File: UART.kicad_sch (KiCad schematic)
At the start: 28 parts, among them J22 430450212, J23 430450612, J24 430450212, J9 Conn_01x03_Pin, U5 MAX485, U7 ISOW1432BDFMR

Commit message: Pre Design Review - Reviewed DRC Errors
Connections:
- net +3V3_TB: now also R20.2
- net +5V_TB: no longer R20.2
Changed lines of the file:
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@@
 			)
 		)
-		(property "Value" "+5V_TB"
+		(property "Value" "+3V3_TB"
 			(at 138.43 81.534 0)
 			(effects

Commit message: Hello Bruh
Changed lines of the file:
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@@
-	)
-	(junction
-		(at 254 107.95)
-		(diameter 0)
-		(color 0 0 0 0)
 	)
 	(junction
@@
 	(junction
 		(at 69.85 77.47)
-		(diameter 0)
-		(color 0 0 0 0)
-	)
-	(junction
-		(at 254 110.49)
 		(diameter 0)
 		(color 0 0 0 0)
@@
 	(wire
 		(pts
-			(xy 254 110.49) (xy 254 114.3)
-		)
-		(stroke
-			(width 0)
-			(type default)
-		)
-	)
-	(wire
-		(pts
 			(xy 123.19 66.04) (xy 129.54 66.04)
 		)
@@
 	(wire
 		(pts
+			(xy 251.46 107.95) (xy 256.54 107.95)
+		)
+		(stroke
+			(width 0)
+			(type default)
+		)
+	)
+	(wire
+		(pts
 			(xy 71.12 116.84) (xy 77.47 116.84)
 		)
@@
 	(wire
 		(pts
-			(xy 251.46 107.95) (xy 254 107.95)
-		)
-		(stroke
-			(width 0)
-			(type default)
-		)
-	)
-	(wire
-		(pts
 			(xy 133.35 113.03) (xy 139.7 113.03)
 		)
@@
 	(wire
 		(pts
-			(xy 254 107.95) (xy 256.54 107.95)
-		)
-		(stroke
-			(width 0)
-			(type default)
-		)
-	)
-	(wire
-		(pts
 			(xy 116.84 91.44) (xy 119.38 91.44)
 		)
@@
 	(wire
 		(pts
-			(xy 254 105.41) (xy 254 107.95)
-		)
-		(stroke
-			(width 0)
-			(type default)
-		)
-	)
-	(wire
-		(pts
 			(xy 173.99 134.62) (xy 175.26 134.62)
 		)
@@
 	(wire
 		(pts
-			(xy 245.11 110.49) (xy 254 110.49)
+			(xy 245.11 110.49) (xy 256.54 110.49)
 		)
 		(stroke
@@
 		(pts
 			(xy 71.12 125.73) (xy 71.12 127)
-		)
-		(stroke
-			(width 0)
-			(type default)
-		)
-	)
-	(wire
-		(pts
-			(xy 254 110.49) (xy 256.54 110.49)
 		)
 		(stroke
@@
 	)
 	(label "A"
-		(at 254 114.3 0)
+		(at 241.3 110.49 0)
 		(fields_autoplaced yes)
 		(effects
@@
 	)
 	(label "B"
-		(at 254 105.41 0)
+		(at 241.3 107.95 0)
 		(fields_autoplaced yes)
 		(effects

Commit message: Fixed MAX485 Schematic
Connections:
- net +5V: now also C14.2, U5.8 (VCC)
- net A: no longer C14.2, U5.8 (VCC)
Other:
- moved on the sheet: R10
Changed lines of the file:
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@@
 	)
 	(junction
+		(at 251.46 87.63)
+		(diameter 0)
+		(color 0 0 0 0)
+	)
+	(junction
 		(at 129.54 73.66)
 		(diameter 0)
@@
 	)
 	(junction
-		(at 245.11 105.41)
-		(diameter 0)
-		(color 0 0 0 0)
-	)
-	(junction
 		(at 119.38 91.44)
 		(diameter 0)
@@
 	(wire
 		(pts
+			(xy 245.11 87.63) (xy 251.46 87.63)
+		)
+		(stroke
+			(width 0)
+			(type default)
+		)
+	)
+	(wire
+		(pts
 			(xy 116.84 71.12) (xy 116.84 73.66)
 		)
@@
 	(wire
 		(pts
-			(xy 238.76 105.41) (xy 245.11 105.41)
+			(xy 238.76 105.41) (xy 251.46 105.41)
 		)
 		(stroke
@@
 	(wire
 		(pts
+			(xy 251.46 83.82) (xy 251.46 87.63)
+		)
+		(stroke
+			(width 0)
+			(type default)
+		)
+	)
+	(wire
+		(pts
 			(xy 77.47 99.06) (xy 77.47 100.33)
 		)
@@
 	(wire
 		(pts
+			(xy 245.11 87.63) (xy 245.11 90.17)
+		)
+		(stroke
+			(width 0)
+			(type default)
+		)
+	)
+	(wire
+		(pts
 			(xy 139.7 114.3) (xy 139.7 113.03)
 		)
@@
 	(wire
 		(pts
-			(xy 116.84 93.98) (xy 116.84 91.44)
+			(xy 251.46 87.63) (xy 251.46 105.41)
 		)
 		(stroke
@@
 	(wire
 		(pts
-			(xy 245.11 110.49) (xy 256.54 110.49)
+			(xy 116.84 93.98) (xy 116.84 91.44)
 		)
 		(stroke
@@
 	(wire
 		(pts
-			(xy 124.46 99.06) (xy 124.46 96.52)
+			(xy 245.11 110.49) (xy 256.54 110.49)
 		)
 		(stroke
@@
 	(wire
 		(pts
-			(xy 201.93 109.22) (xy 201.93 110.49)
+			(xy 124.46 99.06) (xy 124.46 96.52)
 		)
 		(stroke
@@
 	(wire
 		(pts
-			(xy 245.11 82.55) (xy 245.11 87.63)
+			(xy 201.93 109.22) (xy 201.93 110.49)
 		)
 		(stroke
@@
 	(wire
 		(pts
-			(xy 245.11 95.25) (xy 245.11 105.41)
-		)
-		(stroke
-			(width 0)
-			(type default)
-		)
-	)
-	(wire
-		(pts
 			(xy 69.85 77.47) (xy 81.28 77.47)
 		)
@@
 	(wire
 		(pts
-			(xy 245.11 105.41) (xy 245.11 110.49)
+			(xy 245.11 97.79) (xy 245.11 110.49)
 		)
 		(stroke
@@
 	(symbol
 		(lib_id "Device:R_US")
-		(at 245.11 91.44 0)
+		(at 245.11 93.98 0)
+		(mirror y)
 		(unit 1)
 		(exclude_from_sim no)
@@
 		(dnp no)
 		(property "Reference" "R10"
-			(at 240.284 89.916 0)
+			(at 249.936 92.456 0)
 			(effects
 				(font
@@
 		)
 		(property "Value" "10k"
-			(at 240.03 92.456 0)
+			(at 250.19 94.996 0)
 			(effects
 				(font
@@
 		)
 		(property "Footprint" "Resistor_SMD:R_0603_1608Metric_Pad0.98x0.95mm_HandSolder"
-			(at 246.126 91.694 90)
+			(at 244.094 94.234 90)
 			(effects
 				(font
@@
 		)
 		(property "Datasheet" "~"
-			(at 245.11 91.44 0)
+			(at 245.11 93.98 0)
 			(effects
 				(font
@@
 		)
 		(property "Description" "Resistor, US symbol"
-			(at 245.11 91.44 0)
+			(at 245.11 93.98 0)
 			(effects
 				(font
@@
 		)
 		(property "Sim.Device" ""
-			(at 245.11 91.44 0)
+			(at 245.11 93.98 0)
 			(effects
 				(font
@@
 		)
 		(property "Sim.Pins" ""
-			(at 245.11 91.44 0)
+			(at 245.11 93.98 0)
 			(effects
 				(font
@@
 		)
 		(property "Sim.Type" ""
-			(at 245.11 91.44 0)
+			(at 245.11 93.98 0)
 			(effects
 				(font
@@
 	)
 	(symbol
+		(lib_id "power:+5V")
+		(at 251.46 83.82 0)
+		(unit 1)
+		(exclude_from_sim no)
+		(in_bom yes)
+		(on_board yes)
+		(dnp no)
+		(fields_autoplaced yes)
+		(property "Reference" "#PWR041"
+			(at 251.46 87.63 0)
+			(effects
+				(font
+					(size 1.27 1.27)
+				)
+				(hide yes)
+			)
+		)
+		(property "Value" "+5V"
+			(at 251.46 78.74 0)
+			(effects
+				(font
+					(size 1.27 1.27)
+				)
+			)
+		)
+		(property "Footprint" ""
+			(at 251.46 83.82 0)
+			(effects
+				(font
+					(size 1.27 1.27)
+				)
+				(hide yes)
+			)
+		)
+		(property "Datasheet" ""
+			(at 251.46 83.82 0)
+			(effects
+				(font
+					(size 1.27 1.27)
+				)
+				(hide yes)
+			)
+		)
+		(property "Description" "Power symbol creates a global label with name \"+5V\""
+			(at 251.46 83.82 0)
+			(effects
+				(font
+					(size 1.27 1.27)
+				)
+				(hide yes)
+			)
+		)
+		(pin "1"
+		)
+		(instances
+			(project "X17_Pi_Shield"
+				(path "/9eec1df9-cfd8-4f98-afed-20048a6985e2/7463edb5-e9bc-436d-95e5-c231049e85db"
+					(reference "#PWR041")
+					(unit 1)
+				)
+			)
+		)
+	)
+	(symbol
 		(lib_id "power:GND")
 		(at 265.43 140.97 0)
@@
 					(unit 1)
 				)
-			)
-		)
-	)
-	(symbol
-		(lib_id "power:+5V")
-		(at 245.11 82.55 0)
-		(unit 1)
-		(exclude_from_sim no)
-		(in_bom yes)
-		(on_board yes)
-		(dnp no)
-		(fields_autoplaced yes)
-		(property "Reference" "#PWR067"
-			(at 245.11 86.36 0)
-			(effects
-				(font
-					(size 1.27 1.27)
-				)
-				(hide yes)
-			)
-		)
-		(property "Value" "+5V"
-			(at 245.11 77.47 0)
-			(effects
-				(font
-					(size 1.27 1.27)
-				)
-			)
-		)
-		(property "Footprint" ""
-			(at 245.11 82.55 0)
-			(effects
-				(font
-					(size 1.27 1.27)
-				)
-				(hide yes)
-			)
-		)
-		(property "Datasheet" ""
-			(at 245.11 82.55 0)
-			(effects
-				(font
-					(size 1.27 1.27)
-				)
-				(hide yes)
-			)
-		)
-		(property "Description" "Power symbol creates a global label with name \"+5V\""
-			(at 245.11 82.55 0)
-			(effects
-				(font
-					(size 1.27 1.27)
-				)
-				(hide yes)
-			)
-		)
-		(pin "1"
-		)
-		(instances
-			(project ""
-				(path "/9eec1df9-cfd8-4f98-afed-20048a6985e2/7463edb5-e9bc-436d-95e5-c231049e85db"
-					(reference "#PWR067")
-					(unit 1)
-				)

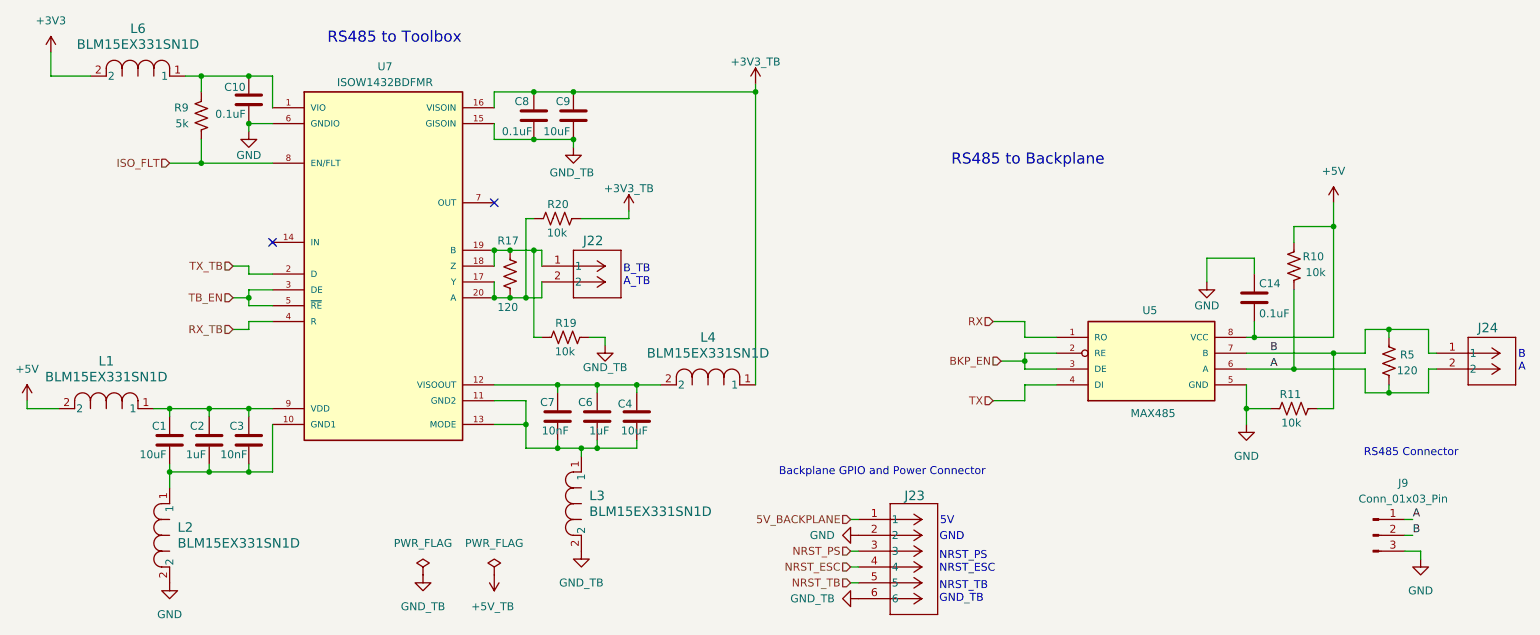
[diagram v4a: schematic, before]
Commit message: fixed several DRC errors and ferrite bead package size, still reviewing the board
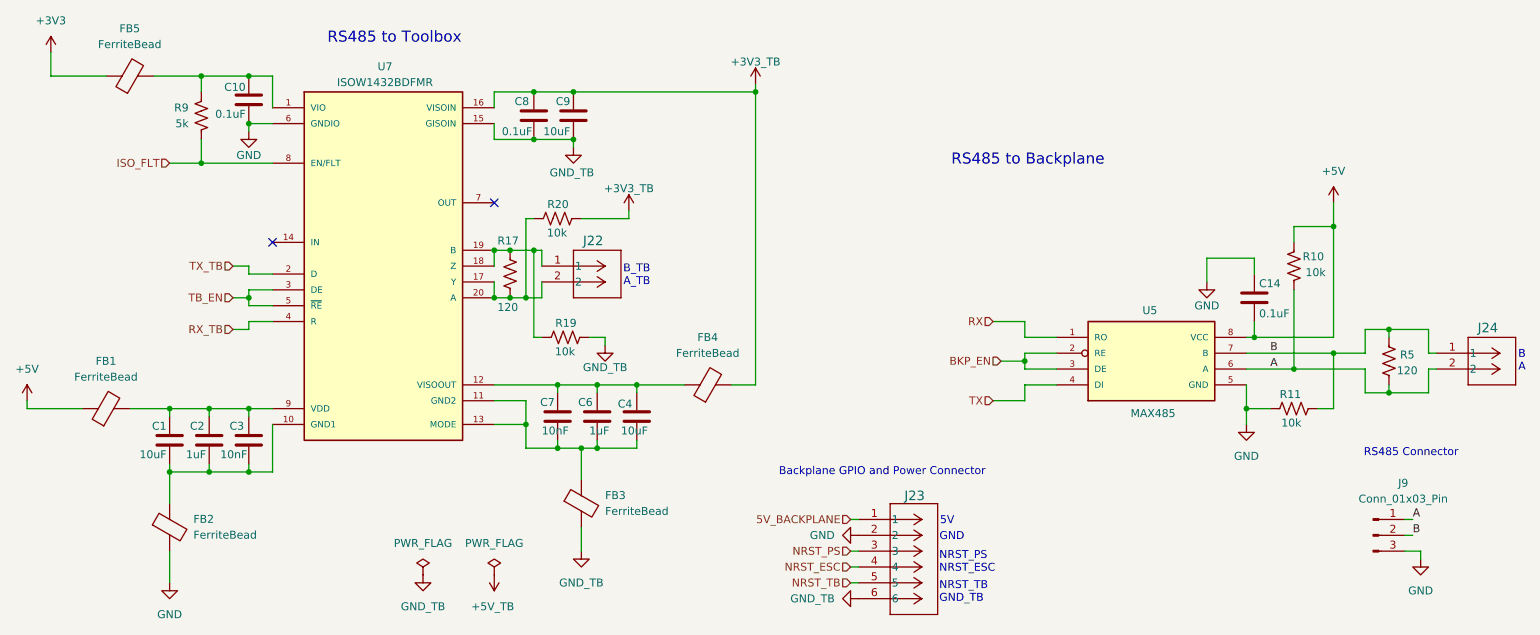
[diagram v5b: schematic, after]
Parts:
- removed L1, L2, L3, L4, L6: BLM15EX331SN1D, BLM15EX331SN1D:IND_BLM15_MUR-M, symbol BLM15EX331SN1D:BLM15EX331SN1D
- added FB1, FB2, FB3, FB4, FB5: FerriteBead, Capacitor_SMD:C_0603_1608Metric_Pad1.08x0.95mm_HandSolder, symbol Device:FerriteBead
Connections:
- net +3V3: now also FB5.1
- net +3V3_TB: now also FB4.2
- net +5V: now also FB1.1
- net GND: now also FB2.2
- net GND_TB: now also FB3.2
- net at C4.2, C6.2, C7.2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: now also FB3.1
- net at C1.1, C2.1, C3.1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: now also FB1.2
- net at C1.2, C2.2, C3.2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: now also FB2.1
- net at C10.2, R9.2, U7.1 (VIO): now also FB5.2
- net at C4.1, C6.1, C7.1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: now also FB4.1
